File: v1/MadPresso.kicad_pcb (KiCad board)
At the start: 2 copper layers, 108 x 57.5 mm, 68 parts, among them J1 Conn_01x07, J2 Conn_01x03, Q1 2N7002, Q2 2N7002, Q3 BC847, Q4 BT138-600, Q5 2N7002, Q6 BT138-600, Q7 2N7002, Q8 BT138-600, Q9 2N7002, U1 LTV-356T, U2 WeMos_D1_mini, U3 TLP160G, U4 TLP160G, U5 TLP160G, U6 MID400, U7 MID400

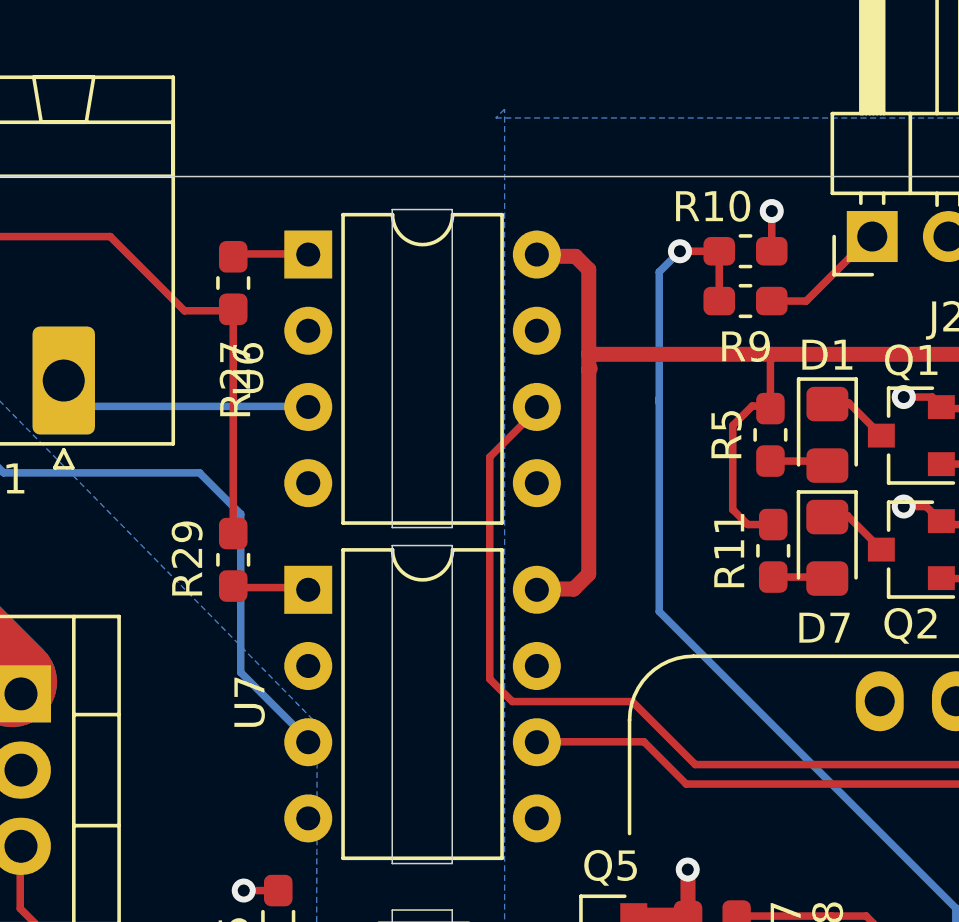
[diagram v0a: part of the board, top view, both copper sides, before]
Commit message: add vaux cap to mid400
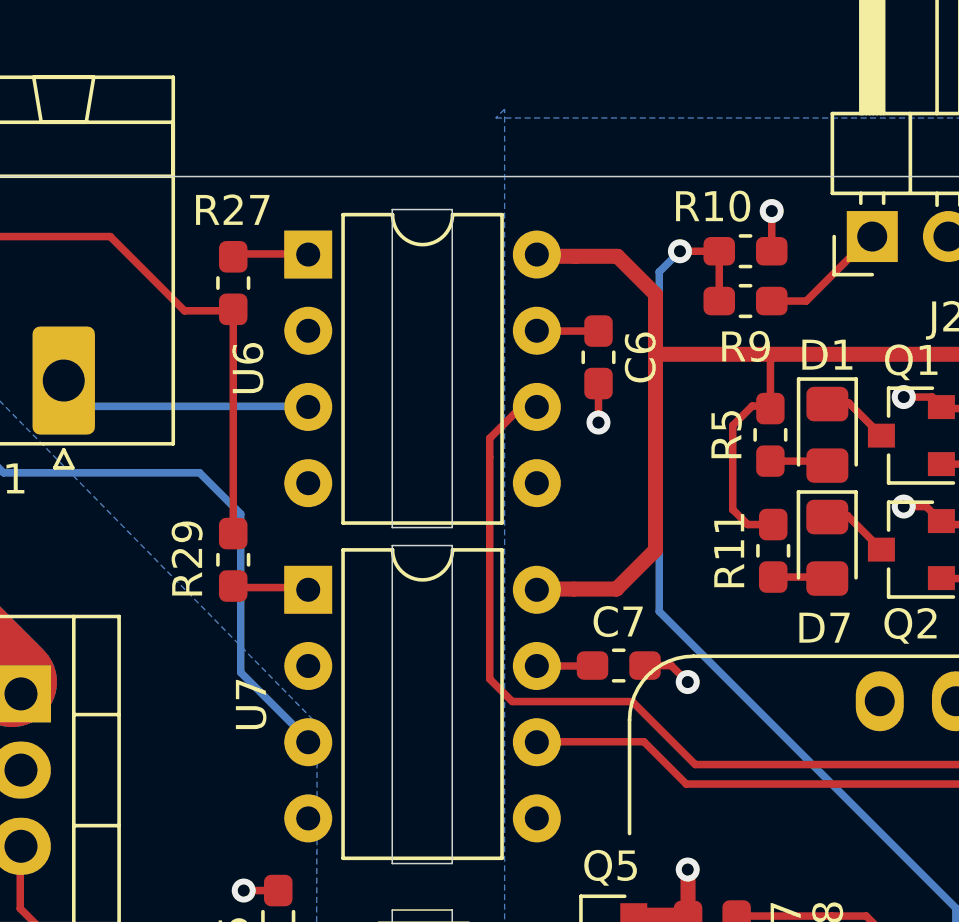
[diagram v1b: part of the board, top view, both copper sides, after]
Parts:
- added C6: DNP, Capacitor_SMD:C_0603_1608Metric_Pad1.05x0.95mm_HandSolder, F.Cu at (71.9, 6.03)
- added C7: DNP, Capacitor_SMD:C_0603_1608Metric_Pad1.05x0.95mm_HandSolder, F.Cu at (72.5, 16.3)
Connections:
- U6 pad 5: GND -> (no net)
- U6 pad 7: (no net) -> Net-(C6-Pad1)
- U6 pad 8: +5V -> (no net)
- U7 pad 5: GND -> (no net)
- U7 pad 7: (no net) -> Net-(C7-Pad1)
- U7 pad 8: +5V -> (no net)
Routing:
- net GND: track 69.5 -> 72.5 mm, vias 11 -> 13
- net Net-(C6-Pad1): track 0.00 -> 2.10 mm
- net Net-(C7-Pad1): track 0.00 -> 1.84 mm
- net +5V: track 185.5 -> 186.7 mm

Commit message: silkscreen
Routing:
- net Net-(C2-Pad1): track 62.3 -> 63.0 mm
- net LINE: track 5.70 -> 6.25 mm
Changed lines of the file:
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@@
     (property "Sheet name" "Valve Triac")
     (attr through_hole)
-    (fp_text reference "Q8" (at -1.8 2.35 90) (layer "F.SilkS")
+    (fp_text reference "Q8" (at 2.555 -4.25 90) (layer "F.SilkS")
       (effects (font (size 1 1) (thickness 0.15)))
     )
@@
     (property "Sheet name" "Pump Triac")
     (attr through_hole)
-    (fp_text reference "Q6" (at -1.8 2.35 90) (layer "F.SilkS")
+    (fp_text reference "Q6" (at 2.53 -4.275 90) (layer "F.SilkS")
       (effects (font (size 1 1) (thickness 0.15)))
     )
@@
     (property "Sheet name" "Pump Triac")
     (attr smd)
-    (fp_text reference "R19" (at -1.375 -1.5 90) (layer "F.SilkS")
+    (fp_text reference "R19" (at 0.025 -1.5 90) (layer "F.SilkS")
       (effects (font (size 1 1) (thickness 0.15)))
     )
@@
     (property "Sheet name" "")
     (attr smd)
-    (fp_text reference "R7" (at 2.656 -0.464) (layer "F.SilkS")
+    (fp_text reference "R7" (at 2.699414 0.017) (layer "F.SilkS")
       (effects (font (size 1 1) (thickness 0.15)))
     )
@@
     (property "Sheet name" "Heater Triac")
     (attr through_hole)
-    (fp_text reference "Q4" (at -1.75 2.4 90) (layer "F.SilkS")
+    (fp_text reference "Q4" (at 2.555 -4.275 90) (layer "F.SilkS")
       (effects (font (size 1 1) (thickness 0.15)))
     )
@@
     (property "Sheet name" "")
     (attr smd)
-    (fp_text reference "C2" (at 3.1 -1.95 180) (layer "F.SilkS")
+    (fp_text reference "C2" (at 0 3.2 270) (layer "F.SilkS")
       (effects (font (size 1 1) (thickness 0.15)))
     )
@@
   (segment (start 98.575 37.275) (end 98.575 35.625) (width 0.25) (layer "F.Cu") (net 5))
   (segment (start 98.625 35.575) (end 98.625 33.85) (width 0.25) (layer "F.Cu") (net 5))
+  (segment (start 61.15 37.1) (end 61.15 35.625) (width 0.25) (layer "F.Cu") (net 6))
   (segment (start 60.05 23.8) (end 61.15 23.8) (width 0.25) (layer "F.Cu") (net 6))
-  (segment (start 61.15 37.1) (end 61.15 35.9) (width 0.25) (layer "F.Cu") (net 6))
+  (segment (start 61.2 30.575) (end 61.2 29.1) (width 0.25) (layer "F.Cu") (net 6))
   (segment (start 20.675 17.85) (end 20.675 16.55) (width 0.25) (layer "F.Cu") (net 6))
   (segment (start 61.2 30.55) (end 61.25 30.6) (width 0.25) (layer "F.Cu") (net 6))
   (segment (start 20.675 16.55) (end 21 16.225) (width 0.25) (layer "F.Cu") (net 6))
-  (segment (start 60.05 30.55) (end 61.2 30.55) (width 0.25) (layer "F.Cu") (net 6))
   (segment (start 61.15 23.8) (end 61.2 23.75) (width 0.25) (layer "F.Cu") (net 6))
   (via (at 21 16.225) (size 0.8) (drill 0.4) (layers "F.Cu" "B.Cu") (net 6))
-  (via (at 60.05 30.55) (size 0.8) (drill 0.4) (layers "F.Cu" "B.Cu") (net 6))
+  (via (at 61.2 29.1) (size 0.8) (drill 0.4) (layers "F.Cu" "B.Cu") (net 6))
   (via (at 60.05 23.8) (size 0.8) (drill 0.4) (layers "F.Cu" "B.Cu") (net 6))
-  (via (at 61.15 35.9) (size 0.8) (drill 0.4) (layers "F.Cu" "B.Cu") (net 6))
-  (segment (start 60.05 30.6) (end 60.05 30.55) (width 0.25) (layer "B.Cu") (net 6))
+  (via (at 61.15 35.625) (size 0.8) (drill 0.4) (layers "F.Cu" "B.Cu") (net 6))
   (segment (start 5.8 10.6) (end 6.1 10.6) (width 2) (layer "B.Cu") (net 6))
   (segment (start 46.525 14.1) (end 49.575 14.1) (width 3) (layer "F.Cu") (net 7))
@@
   (segment (start 18.279 28.297) (end 20.247 28.297) (width 0.25) (layer "F.Cu") (net 20))
   (segment (start 17.272 28.297) (end 17.2 28.225) (width 0.25) (layer "F.Cu") (net 20))
+  (segment (start 58.9 45.775) (end 58.9 44.65) (width 0.25) (layer "F.Cu") (net 20))
   (segment (start 19.7 37.05) (end 19.8 37.15) (width 0.25) (layer "F.Cu") (net 20))
   (segment (start 41.9 46.5) (end 57.3 46.5) (width 0.25) (layer "F.Cu") (net 20))
+  (segment (start 58.175 46.5) (end 58.9 45.775) (width 0.25) (layer "F.Cu") (net 20))
   (segment (start 20.7 34.5) (end 19.65 34.5) (width 0.25) (layer "F.Cu") (net 20))
   (segment (start 21.3 33.9) (end 20.7 34.5) (width 0.25) (layer "F.Cu") (net 20))
   (segment (start 58.9 44.65) (end 58.9 44.9) (width 0.25) (layer "F.Cu") (net 20))
   (segment (start 21.7 39.05) (end 19.8 37.15) (width 0.25) (layer "F.Cu") (net 20))
+  (segment (start 57.3 46.5) (end 58.175 46.5) (width 0.25) (layer "F.Cu") (net 20))
   (segment (start 19.7 34.4) (end 19.7 37.05) (width 0.25) (layer "F.Cu") (net 20))
   (segment (start 15.993 26.048) (end 18.279 26.048) (width 0.25) (layer "F.Cu") (net 20))
@@
   (segment (start 18.279 28.297) (end 17.272 28.297) (width 0.25) (layer "F.Cu") (net 20))
   (segment (start 21.7 39.05) (end 34.45 39.05) (width 0.25) (layer "F.Cu") (net 20))
-  (segment (start 58.9 44.9) (end 57.3 46.5) (width 0.25) (layer "F.Cu") (net 20))
   (segment (start 76.26 38.045) (end 84.245 38.045) (width 0.25) (layer "F.Cu") (net 21))
   (segment (start 76.26 38.045) (end 76.505 37.8) (width 0.25) (layer "F.Cu") (net 21))

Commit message: cleanups
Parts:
- moved R26 0.26 mm to (76.5, 38.9)
- moved R25 0.25 mm to (74.9, 38.9)
- moved R11 0.10 mm to (77.6, 12.5)
- moved R2 0.10 mm to (85.0, 8.63)
- moved R1 0.10 mm to (86.6, 8.62)
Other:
- board text added: "PCB outline for Hammond 1591XXB case"

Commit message: Move PCB outline and screw holes to footprint
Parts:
- added REF**: Hammond 1591XXB, MadPresso:Hammond 1591XXB, F.Cu at (0.00, 0.00)
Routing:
- net +5V: track 186.6 -> 187.2 mm
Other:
- outline, holes or cut-outs redrawn
- board text removed: "PCB outline for Hammond 1591XXB case"
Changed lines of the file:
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@@
     (property "Sheet name" "")
     (attr smd)
-    (fp_text reference "D9" (at 0.05 3.2 90) (layer "F.SilkS")
+    (fp_text reference "D9" (at -4.53 0.04 180) (layer "F.SilkS")
       (effects (font (size 1 1) (thickness 0.15)))
     )
@@
     )
   )
+  (module "MadPresso:Hammond 1591XXB" locked (layer "F.Cu")
+    (at 0 0)
+    (descr "Hammond 1591XXB plastic casing")
+    (tags "https://www.hammfg.com/part/1591XXFBK")
+    (attr smd board_only)
+    (fp_text reference "REF**" (at 57.45 60.75 unlocked) (layer "F.SilkS") hide
+      (effects (font (size 1 1) (thickness 0.15)))
+    )
+    (fp_text value "Hammond 1591XXB" (at -0.98 36.35 90 unlocked) (layer "F.Fab")
+      (effects (font (size 1 1) (thickness 0.15)))
+    )
+    (fp_circle (center 92.75 47) (end 95.75 47) (layer "F.SilkS") (width 0.12))
+    (fp_circle (center 15.25 47) (end 18.25 47) (layer "F.SilkS") (width 0.12))
+    (fp_circle (center 15.25 10.5) (end 18.25 10.5) (layer "F.SilkS") (width 0.12))
+    (fp_circle (center 92.75 10.5) (end 95.75 10.5) (layer "F.SilkS") (width 0.12))
+    (fp_line (start 7.999874 -0.004836) (end 99.999874 -0.004836) (layer "Edge.Cuts") (width 0.05))
+    (fp_line (start 102.999874 49.495164) (end 107.999874 49.495164) (layer "Edge.Cuts") (width 0.05))
+    (fp_line (start 99.999874 4.995164) (end 99.999874 -0.004836) (layer "Edge.Cuts") (width 0.05))
+    (fp_line (start -0.000126 7.995164) (end 4.999874 7.995164) (layer "Edge.Cuts") (width 0.05))
+    (fp_line (start 107.999874 7.995164) (end 102.999874 7.995164) (layer "Edge.Cuts") (width 0.05))
+    (fp_line (start 4.999874 49.495164) (end -0.000126 49.495164) (layer "Edge.Cuts") (width 0.05))
+    (fp_line (start 7.999874 57.495164) (end 7.999874 52.495164) (layer "Edge.Cuts") (width 0.05))
+    (fp_line (start -0.000126 7.995164) (end -0.000126 49.495164) (layer "Edge.Cuts") (width 0.05))
+    (fp_line (start 7.999874 -0.004836) (end 7.999874 4.995164) (layer "Edge.Cuts") (width 0.05))
+    (fp_line (start 99.999874 57.495164) (end 99.999874 52.495164) (layer "Edge.Cuts") (width 0.05))
+    (fp_line (start 107.999874 7.995164) (end 107.999874 49.495164) (layer "Edge.Cuts") (width 0.05))
+    (fp_line (start 7.999874 57.495164) (end 99.999874 57.495164) (layer "Edge.Cuts") (width 0.05))
+    (fp_arc (start 4.999874 52.495164) (end 7.999874 52.495164) (angle -90) (layer "Edge.Cuts") (width 0.05))
+    (fp_arc (start 102.999874 52.495164) (end 102.999874 49.495164) (angle -90) (layer "Edge.Cuts") (width 0.05))
+    (fp_arc (start 102.999874 4.995164) (end 99.999874 4.995164) (angle -90) (layer "Edge.Cuts") (width 0.05))
+    (fp_arc (start 4.999874 4.995164) (end 4.999874 7.995164) (angle -90) (layer "Edge.Cuts") (width 0.05))
+    (pad "" np_thru_hole circle (at 15.25 10.5) (size 3.5 3.5) (drill 3.5) (layers *.Mask)
+      (solder_mask_margin 2) (clearance 2))
+    (pad "" np_thru_hole circle (at 92.75 10.5) (size 3.5 3.5) (drill 3.5) (layers *.Mask)
+      (solder_mask_margin 2) (clearance 2))
+    (pad "" np_thru_hole circle (at 92.75 47) (size 3.5 3.5) (drill 3.5) (layers *.Mask)
+      (solder_mask_margin 2) (clearance 2))
+    (pad "" np_thru_hole circle (at 15.25 47) (size 3.5 3.5) (drill 3.5) (layers *.Mask)
+      (solder_mask_margin 2) (clearance 2))
+  )
   (module "Module:WEMOS_D1_mini_light" (layer "F.Cu")
     (at 81.25 40.35 90)
@@
   (gr_circle (center 11 55) (end 11.3 55) (layer "F.Mask") (width 1))
   (gr_circle (center 11 3) (end 11.3 3) (layer "F.Mask") (width 1))
-  (gr_circle (center 15.25 10.5) (end 18.75 10.5) (layer "Dwgs.User") (width 0.15))
-  (gr_circle (center 15.25 47) (end 18.75 47) (layer "Dwgs.User") (width 0.15))
-  (gr_circle (center 92.75 47) (end 96.25 47) (layer "Dwgs.User") (width 0.15))
-  (gr_circle (center 92.75 10.5) (end 96.25 10.5) (layer "Dwgs.User") (width 0.15))
-  (gr_line (start 8 57.5) (end 100 57.5) (layer "Edge.Cuts") (width 0.05))
-  (gr_line (start 0 8) (end 0 49.5) (layer "Edge.Cuts") (width 0.05))
-  (gr_arc (start 103 5) (end 100 5) (angle -90) (layer "Edge.Cuts") (width 0.05))
-  (gr_line (start 108 8) (end 103 8) (layer "Edge.Cuts") (width 0.05))
-  (gr_line (start 100 5) (end 100 0) (layer "Edge.Cuts") (width 0.05))
-  (gr_line (start 100 57.5) (end 100 52.5) (layer "Edge.Cuts") (width 0.05))
-  (gr_line (start 103 49.5) (end 108 49.5) (layer "Edge.Cuts") (width 0.05))
-  (gr_line (start 5 49.5) (end 0 49.5) (layer "Edge.Cuts") (width 0.05))
-  (gr_line (start 8 57.5) (end 8 52.5) (layer "Edge.Cuts") (width 0.05))
-  (gr_line (start 0 8) (end 5 8) (layer "Edge.Cuts") (width 0.05))
-  (gr_line (start 8 0) (end 8 5) (layer "Edge.Cuts") (width 0.05))
   (gr_circle (center 92.75 47) (end 94.5 47) (layer "Edge.Cuts") (width 0.05))
-  (gr_circle (center 15.25 10.5) (end 17 10.5) (layer "Edge.Cuts") (width 0.05))
   (gr_circle (center 15.25 47) (end 17 47) (layer "Edge.Cuts") (width 0.05))
   (gr_line (start 67 42.5) (end 65 42.5) (layer "Edge.Cuts") (width 0.05))
@@
   (gr_line (start 66.975 43.575) (end 66.975 48.275) (layer "Edge.Cuts") (width 0.05))
   (gr_line (start 67 35.9) (end 65 35.9) (layer "Edge.Cuts") (width 0.05))
-  (gr_arc (start 5 52.5) (end 8 52.5) (angle -90) (layer "Edge.Cuts") (width 0.05))
-  (gr_arc (start 103 52.5) (end 103 49.5) (angle -90) (layer "Edge.Cuts") (width 0.05))
-  (gr_line (start 108 8) (end 108 49.5) (layer "Edge.Cuts") (width 0.05))
   (gr_line (start 64.975 43.575) (end 66.975 43.575) (layer "Edge.Cuts") (width 0.05))
   (gr_line (start 64.975 48.275) (end 64.975 43.575) (layer "Edge.Cuts") (width 0.05))
   (gr_circle (center 92.75 10.5) (end 94.5 10.5) (layer "Edge.Cuts") (width 0.05))
   (gr_line (start 66.975 48.275) (end 64.975 48.275) (layer "Edge.Cuts") (width 0.05))
-  (gr_arc (start 5 5) (end 5 8) (angle -90) (layer "Edge.Cuts") (width 0.05))
   (gr_line (start 67 11.7) (end 65 11.7) (layer "Edge.Cuts") (width 0.05))
   (gr_line (start 65 11.7) (end 65 1.1) (layer "Edge.Cuts") (width 0.05))
-  (gr_line (start 8 0) (end 100 0) (layer "Edge.Cuts") (width 0.05))
   (gr_line (start 65 35.9) (end 65 31.2) (layer "Edge.Cuts") (width 0.05))
   (gr_line (start 67 31.2) (end 67 35.9) (layer "Edge.Cuts") (width 0.05))
@@
     (effects (font (size 1.5 1.5) (thickness 0.3)))
   )
-  (gr_text "PCB outline for Hammond 1591XXB case" (at 17.08 67.48) (layer "F.Fab")
-    (effects (font (size 1 1) (thickness 0.15)))
-  )
   (dimension (type aligned) (layer "F.Fab")
     (pts (xy 0 49.5) (xy 108 49.5))
@@
   (segment (start 98.8 10.925) (end 98.725 11) (width 0.25) (layer "F.Cu") (net 11))
   (segment (start 73.05 35) (end 72.05 36) (width 0.25) (layer "F.Cu") (net 11))
-  (segment (start 86.2 51.2) (end 95.55 51.2) (width 1) (layer "F.Cu") (net 11))
   (segment (start 77.605 5.97) (end 77.65 5.925) (width 0.25) (layer "F.Cu") (net 11))
   (segment (start 102.675 10.925) (end 98.8 10.925) (width 0.25) (layer "F.Cu") (net 11))
@@
   (segment (start 99.12 47.63) (end 103.15 43.6) (width 1) (layer "F.Cu") (net 11))
   (segment (start 73.05 28.6) (end 72.05 29.6) (width 0.25) (layer "F.Cu") (net 11))
+  (segment (start 94.84 51.91) (end 87 51.91) (width 1) (layer "F.Cu") (net 11))
   (segment (start 103.15 43.6) (end 103.15 21.475) (width 1) (layer "F.Cu") (net 11))
   (segment (start 75.5 56.1) (end 76 55.6) (width 1) (layer "F.Cu") (net 11))
@@
   (segment (start 72.51 2.66) (end 73.775 3.925) (width 0.5) (layer "F.Cu") (net 11))
   (segment (start 99.275 17.15) (end 99.125 17.3) (width 0.25) (layer "F.Cu") (net 11))
+  (segment (start 87 51.91) (end 86.19 51.1) (width 1) (layer "F.Cu") (net 11))
   (segment (start 55.3 56.1) (end 73 56.1) (width 1) (layer "F.Cu") (net 11))
   (segment (start 79.1 52.5) (end 81.925 52.5) (width 1) (layer "F.Cu") (net 11))
@@
   (segment (start 73.775 12.45) (end 72.475 13.75) (width 0.5) (layer "F.Cu") (net 11))
   (segment (start 76.35 8.3) (end 76.35 8.225) (width 0.25) (layer "F.Cu") (net 11))
+  (segment (start 95.55 51.2) (end 94.84 51.91) (width 1) (layer "F.Cu") (net 11))
   (segment (start 76.35 11.1) (end 76.35 8.3) (width 0.25) (layer "F.Cu") (net 11))
   (segment (start 81.925 52.5) (end 83.2 51.225) (width 1) (layer "F.Cu") (net 11))

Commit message: cosmetics
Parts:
- R15, R19, R23: footprint Resistor_SMD:R_0603_1608Metric_Pad1.05x0.95mm_HandSolder -> Resistor_SMD:R_1206_3216Metric_Pad1.42x1.75mm_HandSolder
- moved R12 2.38 mm to (59.8, 47.0)
- moved U1 2.38 mm to (66.2, 48.3)
- moved U5 1.65 mm to (66.0, 41.8)
- moved Q9 1.65 mm to (72.0, 40.5)
- moved R24 1.65 mm to (72.1, 43.2)
- moved R25 1.65 mm to (74.9, 40.6)
- moved R26 1.65 mm to (76.5, 40.6)
- moved R21 1.23 mm to (74.9, 33.4)
- moved Q7 1.23 mm to (72.0, 33.5)
- moved R20 1.23 mm to (72.2, 36.1)
- moved R22 1.23 mm to (76.5, 33.4)
- moved U4 1.23 mm to (66.0, 34.8)
- moved R18 0.95 mm to (76.5, 26.5)
- moved U3 0.95 mm to (66.0, 27.8)
- moved Q5 0.95 mm to (72.0, 26.5)
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- renumbered REF** to Case
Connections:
- U6 pad 5: (no net) -> GND
- U6 pad 8: (no net) -> +5V
- U7 pad 5: (no net) -> GND
- U7 pad 8: (no net) -> +5V
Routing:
- net Net-(C2-Pad1): track 63.0 -> 61.3 mm
- net +5V: track 187.2 -> 188.8 mm
- net /HEATER_TRIAC: track 24.5 -> 26.0 mm
- net /ZC_DETECT: track 33.0 -> 34.4 mm
- net Net-(U5-Pad6): track 46.8 -> 48.0 mm
- net Net-(U3-Pad6): track 14.3 -> 15.5 mm
- net Net-(U4-Pad6): track 29.1 -> 28.0 mm
- net Net-(Q3-Pad3): track 54.3 -> 55.2 mm
- net LINE: track 6.12 -> 6.71 mm
- net /PUMP_TRIAC: track 19.2 -> 18.7 mm

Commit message: final touches for v1
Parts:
- J2: footprint Connector_PinHeader_2.54mm:PinHeader_1x03_P2.54mm_Horizontal -> Connector_JST:JST_PH_S3B-PH-K_1x03_P2.00mm_Horizontal
- moved J2 4.94 mm to (85.8, 3.35), turned to 180 degrees
- moved J1 0.30 mm to (54.0, 7.10)
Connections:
- J2 pad 1: Net-(J2-Pad1) -> +5V
- J2 pad 3: +5V -> Net-(J2-Pad3)
- R9 pad 2: Net-(J2-Pad1) -> Net-(J2-Pad3)
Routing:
- net Net-(J2-Pad3): track 0.00 -> 4.43 mm
- net Net-(J2-Pad1): track 4.26 -> 0.00 mm
- net /VALVE: track 24.1 -> 25.2 mm
- net +5V: track 188.8 -> 188.0 mm
- net /STEAM_SW: track 21.6 -> 22.2 mm
